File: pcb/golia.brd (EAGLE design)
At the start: 50 x 33.8 mm, 24 parts, among them IC1 xm64a4u, U1 MCP1825S-3302E/DB, X2 EXT

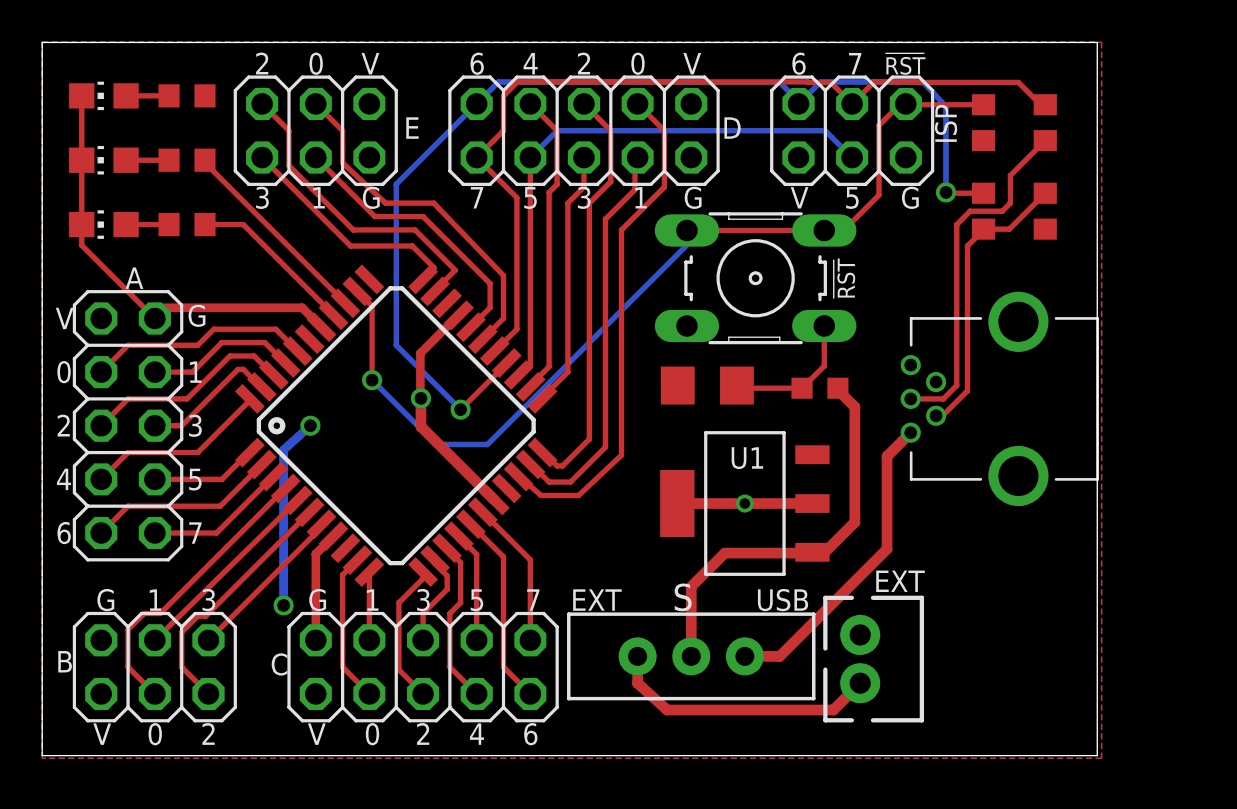
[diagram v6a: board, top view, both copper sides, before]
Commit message: Reduced width and removed !RST pullup
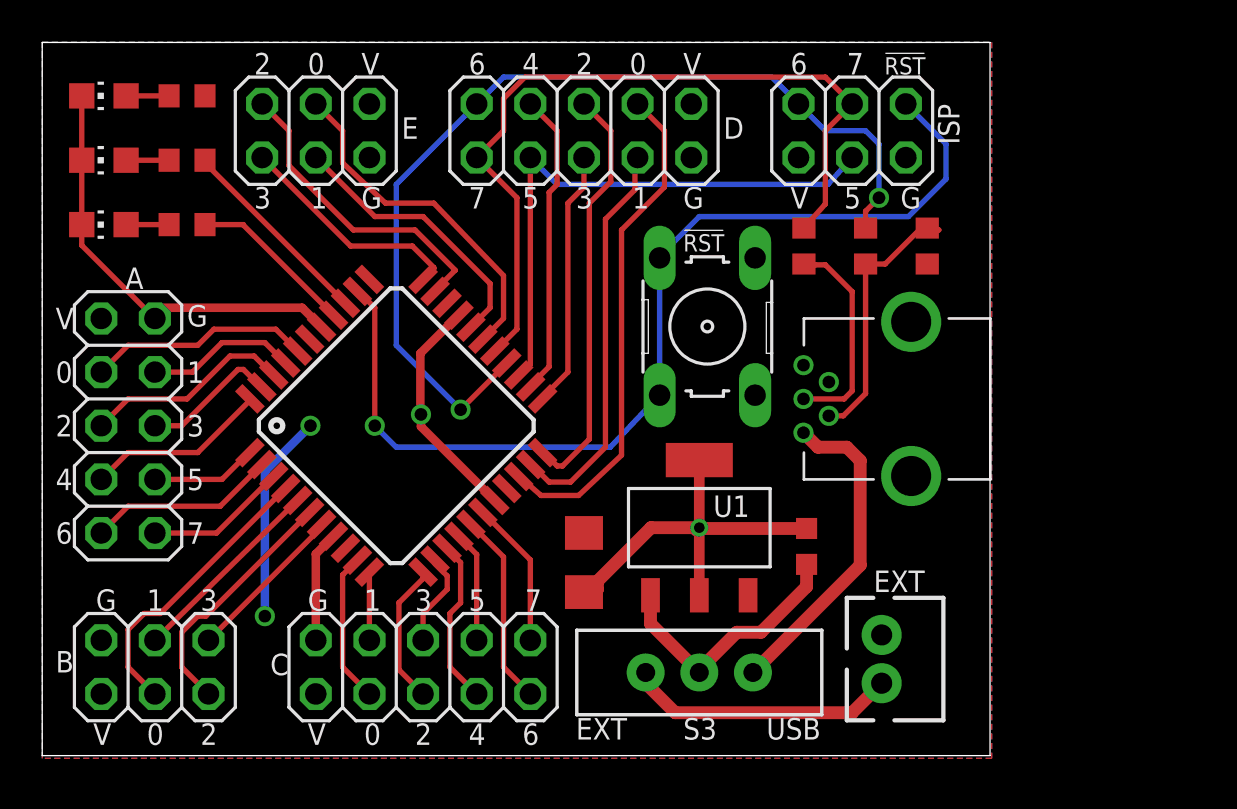
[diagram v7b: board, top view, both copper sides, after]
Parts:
- removed R1: 10K, rcl:R0603
- removed S: 3, Switches:EG-1218
- added S3: S3, Switches:EG-1218
- moved R3 12.8 mm to (35.8, 23.4)
- moved C2 10.2 mm to (25.4, 8.38), turned to 270 degrees
- moved C1 7.52 mm to (35.9, 9.14), turned to 90 degrees
- moved R2 5.83 mm to (41.7, 23.4)
- moved R4 5.83 mm to (38.7, 23.4)
- moved USB 5.08 mm to (40.9, 16.1)
- moved S1 3.23 mm to (31.2, 19.6), turned to 90 degrees
- moved U1 2.44 mm to (30.9, 10.0), turned to 90 degrees
- moved X2 1.02 mm to (39.5, 3.81)
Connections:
- net !RESET: no longer R1.1
- net +3V3: no longer R1.2
- net LED1: now also IC1.36, R7.2; no longer IC1.37, R6.2
- net LED2: now also IC1.37, R6.2; no longer IC1.36, R7.2
- net N$1: now also S3.1; no longer S.1
- net N$2: now also S3.3; no longer S.3
- net N$5: now also S3.2; no longer S.2
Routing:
- net N$4: track 16.7 -> 9.98 mm
- net N$5: track 18.6 -> 12.5 mm
- net GND: track 49.8 -> 55.6 mm
- net PD6: track 50.4 -> 45.6 mm
- net !RESET: track 43.8 -> 47.9 mm
- net PD7: track 41.1 -> 38.0 mm
- net LED1: track 7.88 -> 9.53 mm
- net LED2: track 9.51 -> 7.88 mm
- net +3V3: track 9.07 -> 9.91 mm
- net N$3: track 13.6 -> 13.0 mm
- net N$2: track 14.8 -> 15.4 mm
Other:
- board size 50 x 33.8 mm -> 44.9 x 33.8 mm

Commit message: Reduced width to 42mm, removed USB series resistors
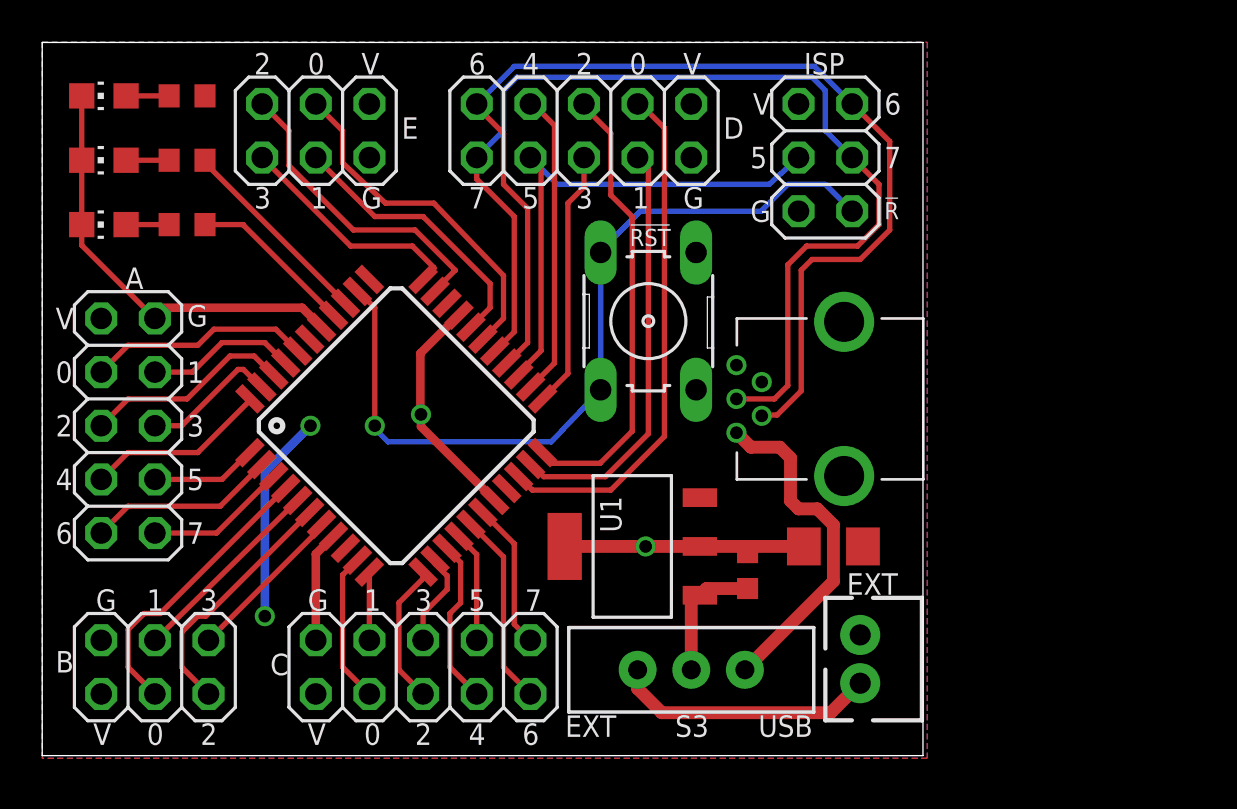
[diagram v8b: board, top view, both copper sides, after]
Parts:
- removed R2: 1.5K, rcl:R0603
- removed R3, R4: 68, rcl:R0603
- moved C2 11.8 mm to (37.2, 9.14), turned to 180 degrees
- moved U1 3.30 mm to (27.7, 9.14), turned to 180 degrees
- moved USB 3.17 mm to (37.7, 16.1)
- moved C1 3.02 mm to (33.1, 8.00)
- moved S1 2.81 mm to (28.4, 19.8)
- moved ISP 1.80 mm to (36.8, 27.6), turned to 270 degrees
- moved X2 1.02 mm to (38.5, 3.81)
- moved S3 0.40 mm to (30.5, 3.30)
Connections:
- removed net N$3: R2.1, R4.1, USB.D-
- removed net N$4: R3.1, USB.D+
- net +3V3: no longer R2.2
- net PD6: now also USB.D-; no longer R4.2
- net PD7: now also USB.D+; no longer R3.2
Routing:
- net N$3: track 13.0 -> 0.00 mm
- net PD7: track 38.0 -> 50.7 mm
- net N$4: track 9.98 -> 0.00 mm
- net !RESET: track 47.9 -> 39.1 mm
- net PD6: track 45.6 -> 52.7 mm, vias 2 -> 0
- net GND: track 55.6 -> 48.5 mm
- net N$5: track 12.5 -> 6.14 mm
- net PD5: track 26.9 -> 24.7 mm
- net PD2: track 19.8 -> 21.5 mm
- net PD1: track 18.9 -> 19.9 mm
- net N$2: track 15.4 -> 16.2 mm
- net PD0: track 24.0 -> 24.6 mm
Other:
- board size 44.9 x 33.8 mm -> 41.7 x 33.8 mm
- board text added: "!R"
